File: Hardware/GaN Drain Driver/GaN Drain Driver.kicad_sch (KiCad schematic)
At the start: 14 parts, among them J1 Conn_Coaxial, Q1 IRFS4321, U1 IRS2005S

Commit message: Started drain driver board
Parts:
- C1: footprint (none) -> Capacitor_SMD:C_0805_2012Metric
- C2, C3, C4, C5, C6, C7, C9: footprint (none) -> Capacitor_THT:CP_Radial_D13.0mm_P5.00mm
- D1: value EGP10B -> 1N5819HW-7-F; footprint (none) -> Diode_SMD:D_SOD-123; Digikey (none) -> BAV19W-E3-08GICT-ND
- J1: footprint (none) -> Connector_Coaxial:SMA_Samtec_SMA-J-P-X-ST-EM1_EdgeMount
- R1, R2: footprint (none) -> Resistor_SMD:R_0805_2012Metric
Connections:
- net AMP_DRAIN: now also C1.2, U1.6 (VS)
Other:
- company: (none) -> openEPR
- title: (none) -> Drain Driver
- moved on the sheet: J1
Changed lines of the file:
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@@
 	(generator_version "8.0")
 	(paper "A4")
+	(title_block
+		(title "Drain Driver")
+		(date "2024-06-18")
+		(rev "v1.0")
+		(company "openEPR")
+		(comment 1 "Timothy Keller")
+	)
 	(junction
 		(at 96.52 63.5)
@@
 	)
 	(junction
+		(at 158.75 68.58)
+		(diameter 0)
+		(color 0 0 0 0)
+	)
+	(junction
 		(at 119.38 49.53)
 		(diameter 0)
@@
 	)
 	(junction
+		(at 129.54 68.58)
+		(diameter 0)
+		(color 0 0 0 0)
+	)
+	(junction
 		(at 129.54 55.88)
 		(diameter 0)
@@
 	(wire
 		(pts
+			(xy 88.9 68.58) (xy 88.9 71.12)
+		)
+		(stroke
+			(width 0)
+			(type default)
+		)
+	)
+	(wire
+		(pts
 			(xy 246.38 48.895) (xy 246.38 50.8)
 		)
@@
 	(wire
 		(pts
-			(xy 158.75 63.5) (xy 158.75 64.77)
+			(xy 158.75 63.5) (xy 158.75 68.58)
 		)
 		(stroke
@@
 	(wire
 		(pts
-			(xy 74.93 68.58) (xy 74.93 71.12)
-		)
-		(stroke
-			(width 0)
-			(type default)
-		)
-	)
-	(wire
-		(pts
 			(xy 107.95 66.04) (xy 107.95 71.12)
 		)
@@
 	(wire
 		(pts
-			(xy 80.01 63.5) (xy 96.52 63.5)
+			(xy 93.98 63.5) (xy 96.52 63.5)
 		)
 		(stroke
@@
 	(wire
 		(pts
-			(xy 158.75 64.77) (xy 161.29 64.77)
+			(xy 158.75 68.58) (xy 161.29 68.58)
 		)
 		(stroke
@@
 		(pts
 			(xy 220.98 55.88) (xy 220.98 57.15)
+		)
+		(stroke
+			(width 0)
+			(type default)
+		)
+	)
+	(wire
+		(pts
+			(xy 129.54 68.58) (xy 158.75 68.58)
 		)
 		(stroke
@@
 	(global_label "AMP_DRAIN"
 		(shape input)
-		(at 161.29 64.77 0)
+		(at 161.29 68.58 0)
 		(fields_autoplaced yes)
 		(effects
@@
 		)
 		(property "Intersheetrefs" "${INTERSHEET_REFS}"
-			(at 174.6167 64.77 0)
+			(at 174.6167 68.58 0)
 			(effects
 				(font
@@
 			)
 		)
-		(property "Footprint" ""
+		(property "Footprint" "Capacitor_THT:CP_Radial_D13.0mm_P5.00mm"
 			(at 233.68 53.34 0)
 			(effects
@@
 			)
 		)
-		(property "Footprint" ""
+		(property "Footprint" "Resistor_SMD:R_0805_2012Metric"
 			(at 96.52 67.31 0)
 			(effects
@@
 	(symbol
 		(lib_id "Connector:Conn_Coaxial")
-		(at 74.93 63.5 0)
+		(at 88.9 63.5 0)
 		(mirror y)
 		(unit 1)
@@
 		(dnp no)
 		(property "Reference" "J1"
-			(at 71.12 62.5231 0)
+			(at 85.09 62.5231 0)
 			(effects
 				(font
@@
 		)
 		(property "Value" "Conn_Coaxial"
-			(at 71.12 65.0631 0)
-			(effects
-				(font
-					(size 1.27 1.27)
-				)
-				(justify left)
-			)
-		)
-		(property "Footprint" ""
-			(at 74.93 63.5 0)
+			(at 85.09 65.0631 0)
+			(effects
+				(font
+					(size 1.27 1.27)
+				)
+				(justify left)
+			)
+		)
+		(property "Footprint" "Connector_Coaxial:SMA_Samtec_SMA-J-P-X-ST-EM1_EdgeMount"
+			(at 88.9 63.5 0)
 			(effects
 				(font
@@
 		)
 		(property "Datasheet" " ~"
-			(at 74.93 63.5 0)
+			(at 88.9 63.5 0)
 			(effects
 				(font
@@
 		)
 		(property "Description" "coaxial connector (BNC, SMA, SMB, SMC, Cinch/RCA, LEMO, ...)"
-			(at 74.93 63.5 0)
+			(at 88.9 63.5 0)
 			(effects
 				(font
@@
 			)
 		)
-		(property "Footprint" ""
+		(property "Footprint" "Capacitor_THT:CP_Radial_D13.0mm_P5.00mm"
 			(at 105.41 53.34 0)
 			(effects
@@
 	(symbol
 		(lib_id "power:GND")
-		(at 74.93 71.12 0)
+		(at 88.9 71.12 0)
 		(unit 1)
 		(exclude_from_sim no)
@@
 		(dnp no)
 		(property "Reference" "#PWR07"
-			(at 74.93 77.47 0)
+			(at 88.9 77.47 0)
 			(effects
 				(font
@@
 		)
 		(property "Value" "GND"
-			(at 74.93 74.93 0)
+			(at 88.9 74.93 0)
 			(effects
 				(font
@@
 		)
 		(property "Footprint" ""
-			(at 74.93 71.12 0)
+			(at 88.9 71.12 0)
 			(effects
 				(font
@@
 		)
 		(property "Datasheet" ""
-			(at 74.93 71.12 0)
+			(at 88.9 71.12 0)
 			(effects
 				(font
@@
 		)
 		(property "Description" "Power symbol creates a global label with name \"GND\" , ground"
-			(at 74.93 71.12 0)
+			(at 88.9 71.12 0)
 			(effects
 				(font
@@
 			)
 		)
-		(property "Footprint" ""
+		(property "Footprint" "Capacitor_THT:CP_Radial_D13.0mm_P5.00mm"
 			(at 184.15 53.34 0)
 			(effects
@@
 			)
 		)
-		(property "Footprint" ""
+		(property "Footprint" "Capacitor_THT:CP_Radial_D13.0mm_P5.00mm"
 			(at 220.98 53.34 0)
 			(effects
@@
 			)
 		)
-		(property "Footprint" ""
+		(property "Footprint" "Capacitor_THT:CP_Radial_D13.0mm_P5.00mm"
 			(at 208.28 53.34 0)
 			(effects
@@
 			)
 		)
-		(property "Footprint" ""
+		(property "Footprint" "Capacitor_THT:CP_Radial_D13.0mm_P5.00mm"
 			(at 246.38 53.34 0)
 			(effects
@@
 			)
 		)
-		(property "Footprint" ""
+		(property "Footprint" "Capacitor_THT:CP_Radial_D13.0mm_P5.00mm"
 			(at 195.58 53.34 0)
 			(effects
@@
 			)
 		)
-		(property "Footprint" ""
+		(property "Footprint" "Resistor_SMD:R_0805_2012Metric"
 			(at 140.97 58.42 0)
 			(effects
@@
 		(on_board yes)
 		(dnp no)
-		(fields_autoplaced yes)
 		(property "Reference" "D1"
-			(at 125.73 43.18 0)
-			(effects
-				(font
-					(size 1.27 1.27)
-				)
-			)
-		)
-		(property "Value" "EGP10B"
-			(at 125.73 45.72 0)
-			(effects
-				(font
-					(size 1.27 1.27)
-				)
-			)
-		)
-		(property "Footprint" ""
+			(at 130.302 45.466 0)
+			(effects
+				(font
+					(size 1.27 1.27)
+				)
+			)
+		)
+		(property "Value" "1N5819HW-7-F"
+			(at 130.302 47.498 0)
+			(effects
+				(font
+					(size 1.27 1.27)
+				)
+			)
+		)
+		(property "Footprint" "Diode_SMD:D_SOD-123"
 			(at 125.73 49.53 90)
 			(effects
@@
 		)
 		(property "Sim.Pins" "1=K 2=A"
+			(at 125.73 49.53 0)
+			(effects
+				(font
+					(size 1.27 1.27)
+				)
+				(hide yes)
+			)
+		)
+		(property "Digikey" "BAV19W-E3-08GICT-ND"
 			(at 125.73 49.53 0)
 			(effects
@@
 			)
 		)
-		(property "Footprint" ""
+		(property "Footprint" "Capacitor_SMD:C_0805_2012Metric"
 			(at 129.54 63.5 0)
 			(effects

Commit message: Updating drain driver board
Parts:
- added H1, H2, H3, H4: 4-40, _tim-Mounting-Holes:4-40_Hole_Pad, symbol Mechanical:MountingHole_Pad
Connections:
- net GND: now also H1.1, H2.1, H3.1, H4.1

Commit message: Updating drain driver board
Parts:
- added C8: 100nF, Capacitor_SMD:C_0805_2012Metric, symbol Device:C_Small
- added J2, J3, J4: Conn_01x02_Socket, Connector_PinSocket_2.54mm:PinSocket_1x02_P2.54mm_Vertical, symbol Connector:Conn_01x02_Socket
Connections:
- net +15V: now also C8.1, J3.1 (Pin_1)
- net AMP_DRAIN: now also J2.1 (Pin_1)
- net GND: now also C8.2, J2.2 (Pin_2), J3.2 (Pin_2), J4.2 (Pin_2)
- net VCC: now also J4.1 (Pin_1)

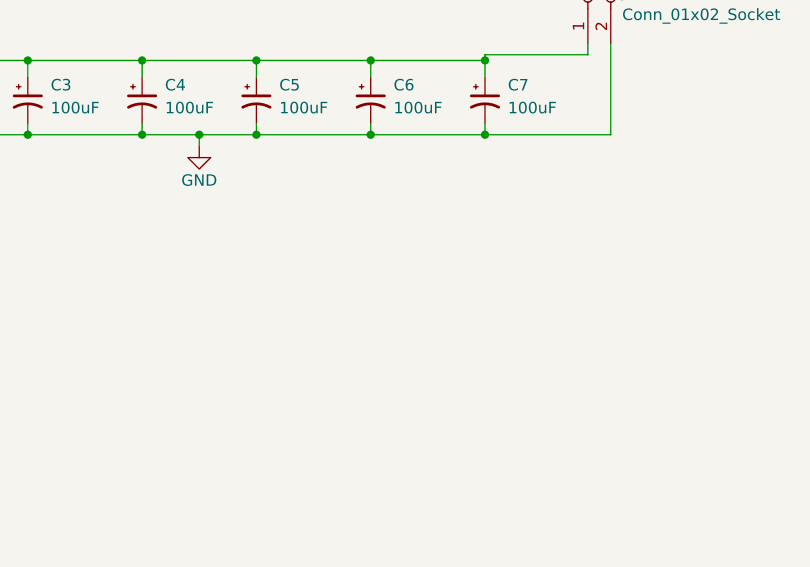
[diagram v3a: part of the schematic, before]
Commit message: Added capacitors
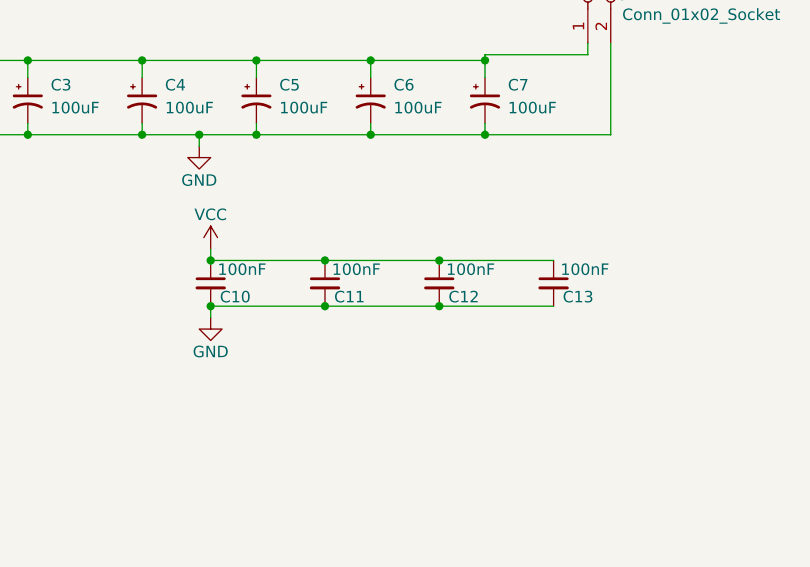
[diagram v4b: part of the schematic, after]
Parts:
- added C10, C11, C12, C13: 100nF, Capacitor_SMD:C_0805_2012Metric, symbol Device:C_Small
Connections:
- net GND: now also C10.2, C11.2, C12.2, C13.2
- net VCC: now also C10.1, C11.1, C12.1, C13.1

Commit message: Adding gerbers
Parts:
- C2, C3, C4, C5, C6, C7, C9: Digikey (none) -> 493-4784-1-ND
- D1: Digikey BAV19W-E3-08GICT-ND -> 1N5819HW-FDICT-ND
- Q1: Digikey (none) -> IRFS4321TRLPBFCT-ND
- U1: Digikey (none) -> IRS2005STRPBFCT-ND
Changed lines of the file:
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@@
+			)
+		)
+		(property "Digikey" "493-4784-1-ND"
+			(at 233.68 53.34 0)
+			(effects
+				(font
+					(size 1.27 1.27)
+				)
+				(hide yes)
 			)
 		)
@@
 			)
 		)
+		(property "Digikey" "493-4784-1-ND"
+			(at 105.41 53.34 0)
+			(effects
+				(font
+					(size 1.27 1.27)
+				)
+				(hide yes)
+			)
+		)
 		(pin "1"
 		)
@@
 			)
 		)
+		(property "Digikey" "493-4784-1-ND"
+			(at 184.15 53.34 0)
+			(effects
+				(font
+					(size 1.27 1.27)
+				)
+				(hide yes)
+			)
+		)
 		(pin "1"
 		)
@@
 			)
 		)
+		(property "Digikey" "493-4784-1-ND"
+			(at 220.98 53.34 0)
+			(effects
+				(font
+					(size 1.27 1.27)
+				)
+				(hide yes)
+			)
+		)
 		(pin "1"
 		)
@@
 			)
 		)
+		(property "Digikey" "493-4784-1-ND"
+			(at 208.28 53.34 0)
+			(effects
+				(font
+					(size 1.27 1.27)
+				)
+				(hide yes)
+			)
+		)
 		(pin "1"
 		)
@@
 			)
 		)
+		(property "Digikey" "493-4784-1-ND"
+			(at 246.38 53.34 0)
+			(effects
+				(font
+					(size 1.27 1.27)
+				)
+				(hide yes)
+			)
+		)
 		(pin "1"
 		)
@@
 		)
 		(property "Description" "High and Low Side Driver, 200V, 290/600mA, SOIC-8"
+			(at 119.38 63.5 0)
+			(effects
+				(font
+					(size 1.27 1.27)
+				)
+				(hide yes)
+			)
+		)
+		(property "Digikey" "IRS2005STRPBFCT-ND"
 			(at 119.38 63.5 0)
 			(effects
@@
 			)
 		)
+		(property "Digikey" "493-4784-1-ND"
+			(at 195.58 53.34 0)
+			(effects
+				(font
+					(size 1.27 1.27)
+				)
+				(hide yes)
+			)
+		)
 		(pin "1"
 		)
@@
 			)
 		)
-		(property "Digikey" "BAV19W-E3-08GICT-ND"
+		(property "Digikey" "1N5819HW-FDICT-ND"
 			(at 125.73 49.53 0)
 			(effects
@@
 			(at 156.21 58.42 0)
 			(effects
+				(font
+					(size 1.27 1.27)
+				)
+				(hide yes)
+			)
+		)
+		(property "Digikey" "IRFS4321TRLPBFCT-ND"
+			(at 156.21 58.42 0)
+			(effects

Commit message: Minor changes
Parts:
- J1: value Conn_Coaxial -> SMA-J-P-H-ST-EM1
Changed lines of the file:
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@@
 			)
 		)
-		(property "Value" "Conn_Coaxial"
+		(property "Value" "SMA-J-P-H-ST-EM1"
 			(at 85.09 65.0631 0)
 			(effects

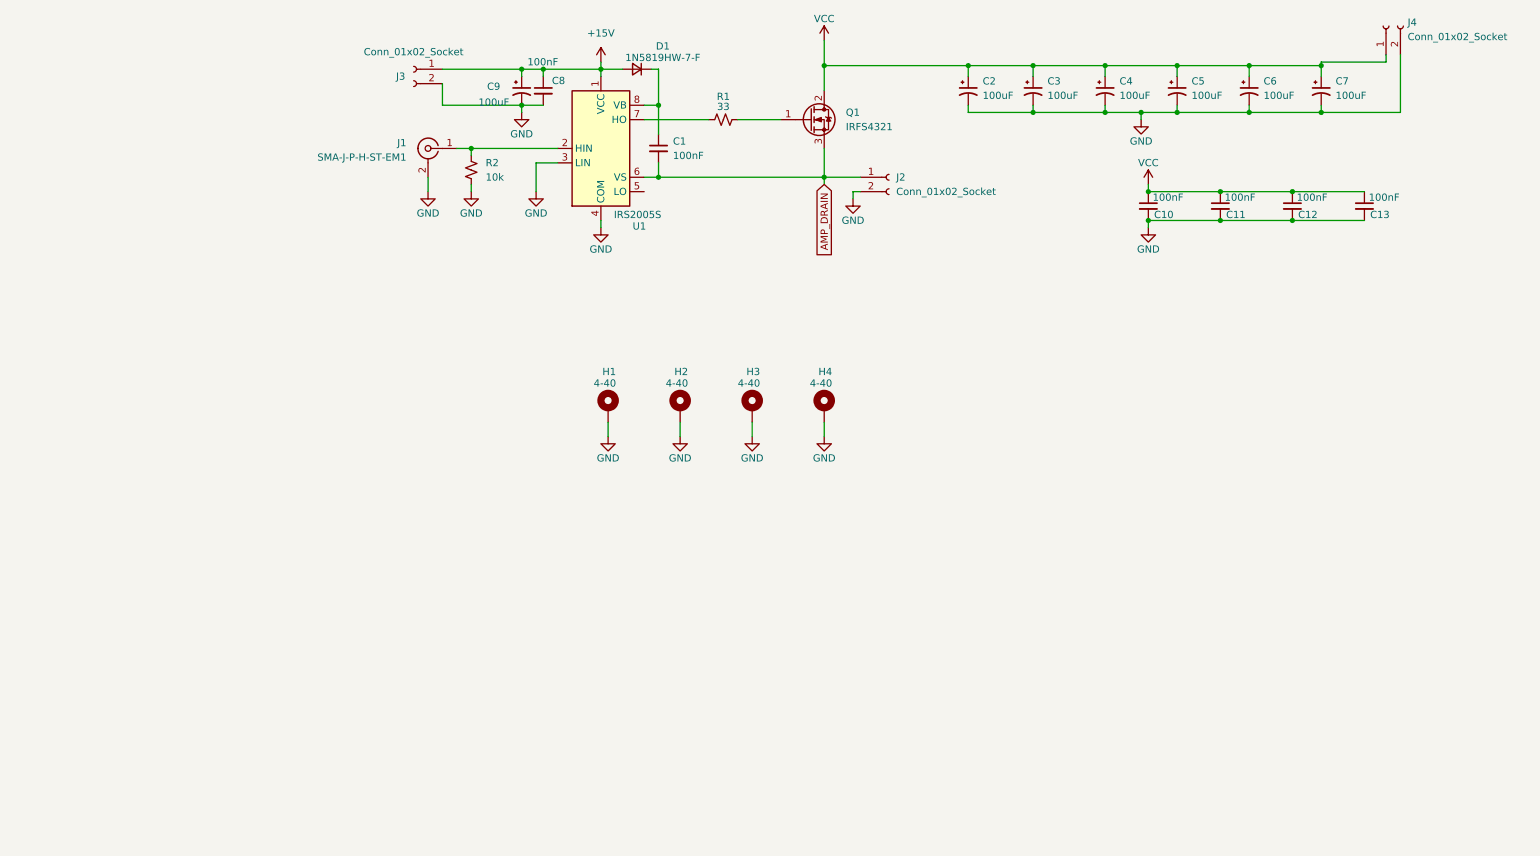
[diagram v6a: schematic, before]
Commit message: Updating Drain Driver PCB
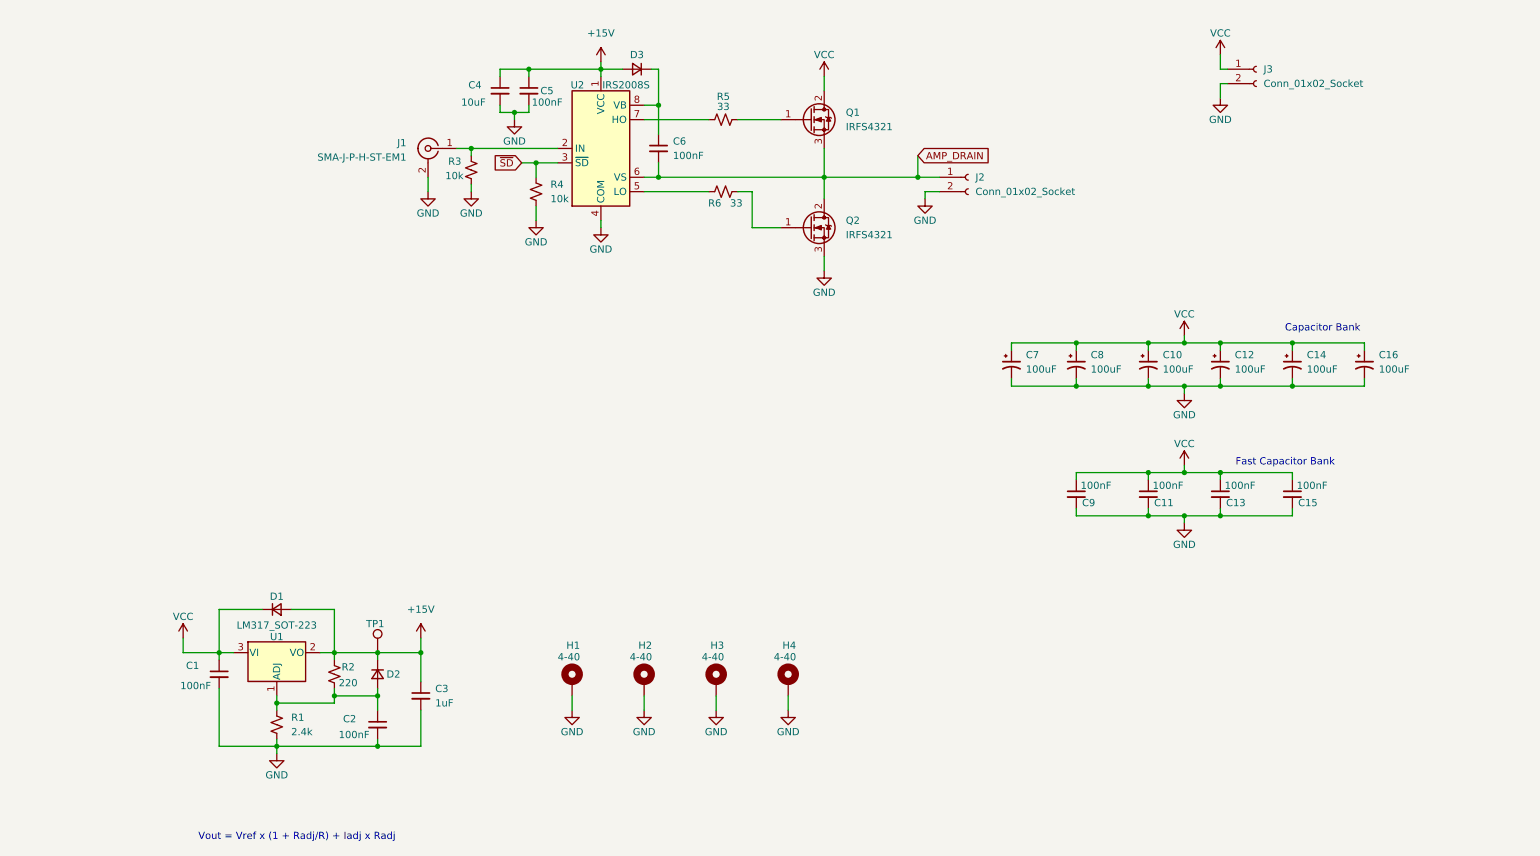
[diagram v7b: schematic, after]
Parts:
- removed C9: 100uF, Capacitor_THT:CP_Radial_D13.0mm_P5.00mm, symbol Device:C_Polarized_Small_US
- removed J3: Conn_01x02_Socket, Connector_PinSocket_2.54mm:PinSocket_1x02_P2.54mm_Vertical, symbol Connector:Conn_01x02_Socket
- removed U1: IRS2005S, Package_SO:SOIC-8_3.9x4.9mm_P1.27mm, symbol Driver_FET:IRS2005S
- added C1, C2: 100nF, Capacitor_SMD:C_0805_2012Metric, symbol Device:C_Small
- added C3: 1uF, Capacitor_SMD:C_0805_2012Metric, symbol Device:C_Small
- added C4: 10uF, Capacitor_SMD:C_0805_2012Metric, symbol Device:C_Small
- added D1, D2: 1N5819HW-7-F, Diode_SMD:D_SOD-123, symbol Device:D_Small
- added Q2: IRFS4321, Package_TO_SOT_SMD:TO-263-2, symbol Transistor_FET:IRFS4321
- added R1: 2.4k, Resistor_SMD:R_0805_2012Metric, symbol Device:R_Small_US
- added R2: 220, Resistor_SMD:R_0805_2012Metric, symbol Device:R_Small_US
- added R4: 10k, Resistor_SMD:R_0805_2012Metric, symbol Device:R_Small_US
- added R6: 33, Resistor_SMD:R_0805_2012Metric, symbol Device:R_Small_US
- added TP1: TestPoint, TestPoint:TestPoint_Pad_D1.0mm, symbol Connector:TestPoint
- added U1: LM317_SOT-223, Package_TO_SOT_SMD:SOT-223-3_TabPin2, symbol Regulator_Linear:LM317_SOT-223
- added U2: IRS2008S, Package_SO:SOIC-8_3.9x4.9mm_P1.27mm, symbol Driver_FET:IRS2008S
- renumbered C4 to C10, C5 to C12, C12 to C13, C6 to C14, C13 to C15, C7 to C16, C8 to C5, C1 to C6, C2 to C7, C3 to C8, C10 to C9, D1 to D3, J4 to J3, R2 to R3, R1 to R5
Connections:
- net +15V: now also C3.1, C4.1, D1.2 (A), D2.1 (K), R2.1, TP1.1, U1.2 (VO), U2.1 (VCC)
- net AMP_DRAIN: now also Q2.2 (D), U2.6 (VS)
- net GND: now also C1.2, C2.2, C3.2, C4.2, Q2.3 (S), R1.2, R4.2, U2.4 (COM)
- net VCC: now also C1.1, D1.1 (K), U1.3 (VI)
- net at J1.1 (In), R3.1: now also U2.2 (IN)
- net at R5.1: now also U2.7 (HO)
- net at C6.1, D3.1 (K): now also U2.8 (VB)
- new net: R6.1, U2.5 (LO)
- new net: C2.1, D2.2 (A), R1.1, R2.2, U1.1 (ADJ)
- new net: Q2.1 (G), R6.2
- new net ~{SD}: R4.1, U2.3 (~{SD})
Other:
- note added: "Capacitor Bank"
- note added: "Fast Capacitor Bank"
- note added: "Vout = Vref x (1 + Radj/R) + Iadj x Radj"
- moved on the sheet: C10, C11, C12, C13, C14, C15, C16, C5, C7, C8, C9, H1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

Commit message: Updating schematic
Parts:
- removed C12, C14, C16: 100uF, Capacitor_THT:CP_Radial_D13.0mm_P5.00mm, symbol Device:C_Polarized_Small_US
- removed C13, C15: 100nF, Capacitor_SMD:C_0805_2012Metric, symbol Device:C_Small
- removed D2: 1N5819HW-7-F, Diode_SMD:D_SOD-123, symbol Device:D_Small
- added R7: 1k, symbol Device:R_Small_US
- added R8: 10k, symbol Device:R_Small_US
- added RV1: 10k, symbol Device:R_Potentiometer_US
- added TP2: TestPoint, symbol Connector:TestPoint
- added U3: LM393, symbol Comparator:LM393
- C10, C7, C8: value 100uF -> 1000uF
- R4: value 10k -> 100k
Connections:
- net VCC: no longer C11.1, C9.1
- new net: RV1.2, TP2.1, U3.2 (-)
- new net +5V: C9.1, R7.1, R8.1, RV1.1, U3.8 (V+)
- new net -5V: C11.1, RV1.3, U3.4 (V-)
- new net GATE_VOLTAGE_GOOD: R7.2, R8.2, U3.1, U3.7
- new net V_gate: U3.3 (+)
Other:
- note added: "Power Requirements: INPUT: 18-36V +15V from regulator +/-5V from switching converter"
- note removed: "Fast Capacitor Bank"
- moved on the sheet: C2, R1
